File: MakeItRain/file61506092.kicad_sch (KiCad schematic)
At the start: 11 parts, among them Q10 2N7000, Q11 2N7000, Q12 IRF9Z34NPBF

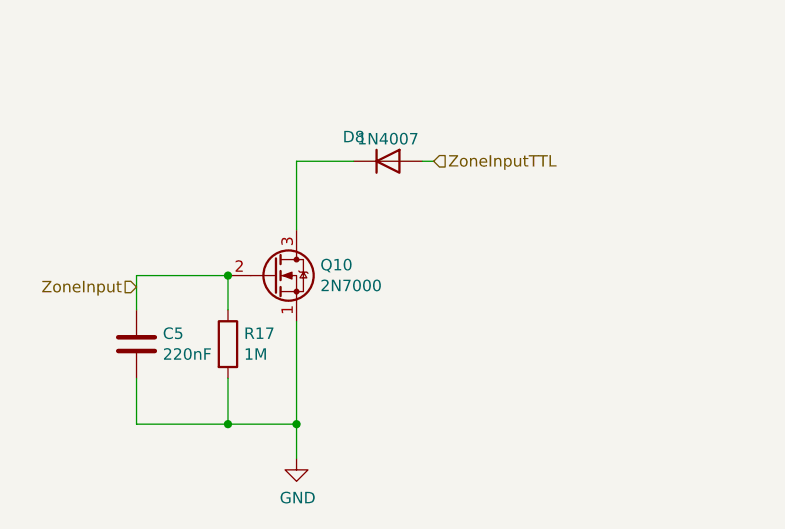
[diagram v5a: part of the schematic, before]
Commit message: working on pin reassignment to fix the stupid stupid ways that esp32 are designed in hardware that require much in way of digging through docs cause not all gpio are created equal.
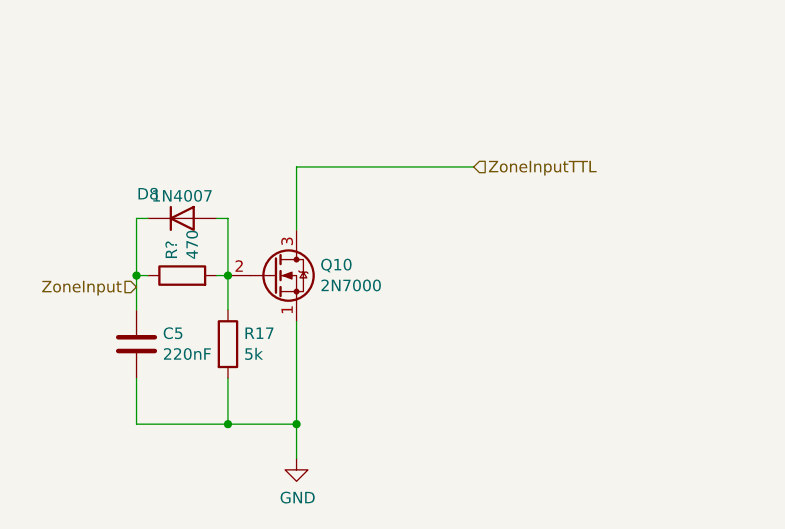
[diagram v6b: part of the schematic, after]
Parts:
- added R?: 470, Resistor_THT:R_Axial_DIN0207_L6.3mm_D2.5mm_P2.54mm_Vertical, symbol Device:R
- R17: value 1M -> 5k
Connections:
- net ZoneInput: now also D8.1 (K), R?.1; no longer Q10.2 (G), R17.1
- net ZoneInputTTL: now also Q10.3 (D); no longer D8.2 (A)
- new net: D8.2 (A), Q10.2 (G), R17.1, R?.2
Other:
- moved on the sheet: D8
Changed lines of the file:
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@@
   (junction (at 125.73 121.92) (diameter 0) (color 0 0 0 0)
   )
+  (junction (at 44.45 76.2) (diameter 0) (color 0 0 0 0)
+  )
   (junction (at 62.23 92.71) (diameter 0) (color 0 0 0 0)
   )
   (junction (at 135.89 55.88) (diameter 0) (color 0 0 0 0)
   )
+  (wire (pts (xy 44.45 76.2) (xy 45.72 76.2))
+    (stroke (width 0) (type default) (color 0 0 0 0))
+  )
   (wire (pts (xy 146.05 55.88) (xy 135.89 55.88))
     (stroke (width 0) (type default) (color 0 0 0 0))
@@
     (stroke (width 0) (type default) (color 0 0 0 0))
   )
-  (wire (pts (xy 62.23 63.5) (xy 62.23 71.12))
-    (stroke (width 0) (type default) (color 0 0 0 0))
-  )
   (wire (pts (xy 125.73 125.73) (xy 125.73 121.92))
     (stroke (width 0) (type default) (color 0 0 0 0))
@@
     (stroke (width 0) (type default) (color 0 0 0 0))
   )
-  (wire (pts (xy 44.45 76.2) (xy 54.61 76.2))
+  (wire (pts (xy 45.72 69.85) (xy 44.45 69.85))
     (stroke (width 0) (type default) (color 0 0 0 0))
   )
@@
     (stroke (width 0) (type default) (color 0 0 0 0))
   )
+  (wire (pts (xy 62.23 71.12) (xy 62.23 64.135))
+    (stroke (width 0) (type default) (color 0 0 0 0))
+  )
   (wire (pts (xy 135.89 55.88) (xy 125.73 55.88))
     (stroke (width 0) (type default) (color 0 0 0 0))
@@
     (stroke (width 0) (type default) (color 0 0 0 0))
   )
+  (wire (pts (xy 62.23 64.135) (xy 81.915 64.135))
+    (stroke (width 0) (type default) (color 0 0 0 0))
+  )
   (wire (pts (xy 142.24 121.92) (xy 125.73 121.92))
     (stroke (width 0) (type default) (color 0 0 0 0))
@@
     (stroke (width 0) (type default) (color 0 0 0 0))
   )
-  (wire (pts (xy 76.2 63.5) (xy 77.47 63.5))
-    (stroke (width 0) (type default) (color 0 0 0 0))
-  )
   (wire (pts (xy 118.11 121.92) (xy 125.73 121.92))
     (stroke (width 0) (type default) (color 0 0 0 0))
   )
-  (wire (pts (xy 68.58 63.5) (xy 62.23 63.5))
+  (wire (pts (xy 53.34 69.85) (xy 54.61 69.85))
+    (stroke (width 0) (type default) (color 0 0 0 0))
+  )
+  (wire (pts (xy 54.61 69.85) (xy 54.61 76.2))
     (stroke (width 0) (type default) (color 0 0 0 0))
   )
@@
   )
   (wire (pts (xy 146.05 92.71) (xy 146.05 90.17))
+    (stroke (width 0) (type default) (color 0 0 0 0))
+  )
+  (wire (pts (xy 44.45 69.85) (xy 44.45 76.2))
+    (stroke (width 0) (type default) (color 0 0 0 0))
+  )
+  (wire (pts (xy 53.34 76.2) (xy 54.61 76.2))
     (stroke (width 0) (type default) (color 0 0 0 0))
   )
@@
     (effects (font (size 1.27 1.27)) (justify left))
   )
-  (hierarchical_label "ZoneInputTTL" (shape input) (at 77.47 63.5 0)
+  (hierarchical_label "ZoneInputTTL" (shape input) (at 81.915 64.135 0)
     (effects (font (size 1.27 1.27)) (justify left))
   )
@@
       (effects (font (size 1.27 1.27)) (justify left))
     )
-    (property "Value" "1M" (id 1) (at 56.388 84.963 0)
+    (property "Value" "5k" (id 1) (at 56.388 84.963 0)
       (effects (font (size 1.27 1.27)) (justify left))
     )
@@
     (pin "2")
   )
-  (symbol (lib_id "Diode:1N4007") (at 72.39 63.5 0)
-    (in_bom yes) (on_board yes)
-    (property "Reference" "D8" (id 0) (at 68.58 60.8035 0))
-    (property "Value" "1N4007" (id 1) (at 72.39 61.0386 0))
-    (property "Footprint" "Diode_THT:D_DO-41_SOD81_P10.16mm_Horizontal" (id 2) (at 72.39 67.945 0)
-      (effects (font (size 1.27 1.27)) hide)
-    )
-    (property "Datasheet" "http://www.vishay.com/docs/88503/1n4001.pdf" (id 3) (at 72.39 63.5 0)
-      (effects (font (size 1.27 1.27)) hide)
-    )
+  (symbol (lib_id "Diode:1N4007") (at 49.53 69.85 0)
+    (in_bom yes) (on_board yes)
+    (property "Reference" "D8" (id 0) (at 45.72 67.1535 0))
+    (property "Value" "1N4007" (id 1) (at 49.53 67.3886 0))
+    (property "Footprint" "Diode_THT:D_DO-41_SOD81_P10.16mm_Horizontal" (id 2) (at 49.53 74.295 0)
+      (effects (font (size 1.27 1.27)) hide)
+    )
+    (property "Datasheet" "http://www.vishay.com/docs/88503/1n4001.pdf" (id 3) (at 49.53 69.85 0)
+      (effects (font (size 1.27 1.27)) hide)
+    )
+    (pin "1")
+    (pin "2")
+  )
+  (symbol (lib_id "Device:R") (at 49.53 76.2 90)
+    (in_bom yes) (on_board yes)
+    (property "Reference" "R?" (id 0) (at 48.3616 74.422 0)
+      (effects (font (size 1.27 1.27)) (justify left))
+    )
+    (property "Value" "470" (id 1) (at 50.673 74.422 0)
+      (effects (font (size 1.27 1.27)) (justify left))
+    )
+    (property "Footprint" "Resistor_THT:R_Axial_DIN0207_L6.3mm_D2.5mm_P2.54mm_Vertical" (id 2) (at 49.53 77.978 90)
+      (effects (font (size 1.27 1.27)) hide)
+    )
+    (property "Datasheet" "~" (id 3) (at 49.53 76.2 0)
+      (effects (font (size 1.27 1.27)) hide)
+    )

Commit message: min updates on schem. wip
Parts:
- gave numbers to parts that had none: 1
- renumbered C5 to C2, D8 to D2, D7 to D3, Q10 to Q1, Q11 to Q2, Q12 to Q3, R17 to R5, R18 to R6, R19 to R7, R20 to R8, Z8 to Z5
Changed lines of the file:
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@@
   (symbol (lib_id "Transistor_FET:2N7000") (at 59.69 76.2 0)
     (in_bom yes) (on_board yes)
-    (property "Reference" "Q10" (id 0) (at 64.8716 75.0316 0)
+    (property "Reference" "Q1" (id 0) (at 64.8716 75.0316 0)
       (effects (font (size 1.27 1.27)) (justify left))
     )
@@
   (symbol (lib_id "Device:R") (at 54.61 83.82 0)
     (in_bom yes) (on_board yes)
-    (property "Reference" "R17" (id 0) (at 56.388 82.6516 0)
+    (property "Reference" "R5" (id 0) (at 56.388 82.6516 0)
       (effects (font (size 1.27 1.27)) (justify left))
     )
@@
   (symbol (lib_id "Transistor_FET:2N7000") (at 123.19 105.41 0)
     (in_bom yes) (on_board yes)
-    (property "Reference" "Q11" (id 0) (at 128.3716 104.2416 0)
+    (property "Reference" "Q2" (id 0) (at 128.3716 104.2416 0)
       (effects (font (size 1.27 1.27)) (justify left))
     )
@@
   (symbol (lib_id "Device:R") (at 118.11 118.11 0)
     (in_bom yes) (on_board yes)
-    (property "Reference" "R18" (id 0) (at 119.888 116.9416 0)
+    (property "Reference" "R6" (id 0) (at 119.888 116.9416 0)
       (effects (font (size 1.27 1.27)) (justify left))
     )
@@
   (symbol (lib_id "Device:R") (at 125.73 91.44 0)
     (in_bom yes) (on_board yes)
-    (property "Reference" "R20" (id 0) (at 127.508 90.2716 0)
+    (property "Reference" "R8" (id 0) (at 127.508 90.2716 0)
       (effects (font (size 1.27 1.27)) (justify left))
     )
@@
   (symbol (lib_id "Device:R") (at 125.73 78.74 0)
     (in_bom yes) (on_board yes)
-    (property "Reference" "R19" (id 0) (at 127.508 77.5716 0)
+    (property "Reference" "R7" (id 0) (at 127.508 77.5716 0)
       (effects (font (size 1.27 1.27)) (justify left))
     )
@@
   (symbol (lib_id "SamacSys_Parts:IRF9Z34NPBF") (at 138.43 85.09 0)
     (in_bom yes) (on_board yes)
-    (property "Reference" "Q12" (id 0) (at 149.352 81.3816 0)
+    (property "Reference" "Q3" (id 0) (at 149.352 81.3816 0)
       (effects (font (size 1.27 1.27)) (justify left))
     )
@@
   (symbol (lib_id "Device:D_Schottky") (at 142.24 101.6 270)
     (in_bom yes) (on_board yes)
-    (property "Reference" "D7" (id 0) (at 144.272 100.4316 90)
+    (property "Reference" "D3" (id 0) (at 144.272 100.4316 90)
       (effects (font (size 1.27 1.27)) (justify left))
     )
@@
   (symbol (lib_id "SamacSys_Parts:BZX79C10") (at 135.89 62.23 90) (mirror x)
     (in_bom yes) (on_board yes)
-    (property "Reference" "Z8" (id 0) (at 139.192 68.6816 90)
+    (property "Reference" "Z5" (id 0) (at 139.192 68.6816 90)
       (effects (font (size 1.27 1.27)) (justify right))
     )
@@
   (symbol (lib_id "Device:C") (at 44.45 83.82 0)
     (in_bom yes) (on_board yes)
-    (property "Reference" "C5" (id 0) (at 47.371 82.6516 0)
+    (property "Reference" "C2" (id 0) (at 47.371 82.6516 0)
       (effects (font (size 1.27 1.27)) (justify left))
     )
@@
   (symbol (lib_id "Diode:1N4007") (at 49.53 69.85 0)
     (in_bom yes) (on_board yes)
-    (property "Reference" "D8" (id 0) (at 45.72 67.1535 0))
+    (property "Reference" "D2" (id 0) (at 45.72 67.1535 0))
     (property "Value" "1N4007" (id 1) (at 49.53 67.3886 0))
     (property "Footprint" "Diode_THT:D_DO-41_SOD81_P10.16mm_Horizontal" (id 2) (at 49.53 74.295 0)
@@
   (symbol (lib_id "Device:R") (at 49.53 76.2 90)
     (in_bom yes) (on_board yes)
-    (property "Reference" "R?" (id 0) (at 48.3616 74.422 0)
-      (effects (font (size 1.27 1.27)) (justify left))
-    )
+    (property "Reference" "R1" (id 0) (at 48.3616 74.422 0)
+      (effects (font (size 1.27 1.27)) (justify left))
+    )

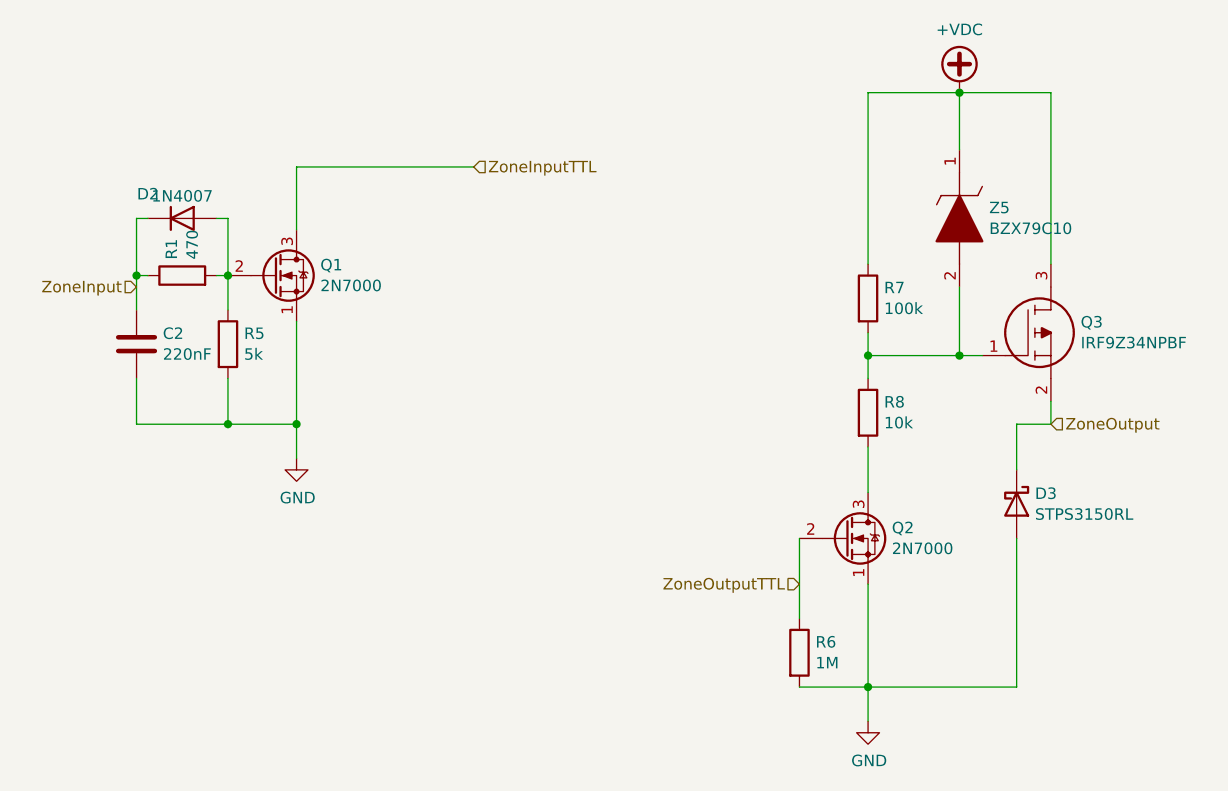
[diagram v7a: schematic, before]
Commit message: starting to add in the mcp23008 to get around the lack of pins or "special" pins that will fuck up designs. stupid ESP32s
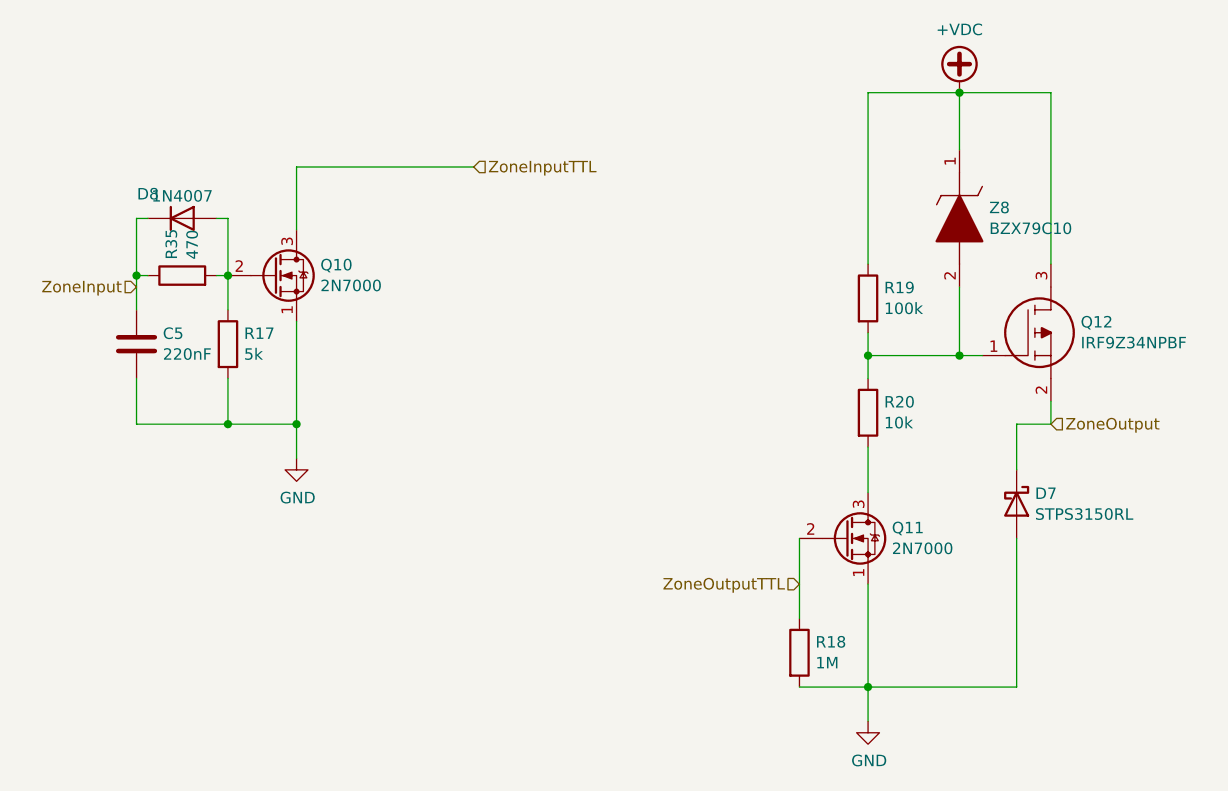
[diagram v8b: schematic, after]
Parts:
- renumbered C2 to C5, D3 to D7, D2 to D8, Q1 to Q10, Q2 to Q11, Q3 to Q12, R5 to R17, R6 to R18, R7 to R19, R8 to R20, R1 to R35, Z5 to Z8
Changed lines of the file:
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@@
   (symbol (lib_id "Transistor_FET:2N7000") (at 59.69 76.2 0)
     (in_bom yes) (on_board yes)
-    (property "Reference" "Q1" (id 0) (at 64.8716 75.0316 0)
+    (property "Reference" "Q10" (id 0) (at 64.8716 75.0316 0)
       (effects (font (size 1.27 1.27)) (justify left))
     )
@@
   (symbol (lib_id "Device:R") (at 54.61 83.82 0)
     (in_bom yes) (on_board yes)
-    (property "Reference" "R5" (id 0) (at 56.388 82.6516 0)
+    (property "Reference" "R17" (id 0) (at 56.388 82.6516 0)
       (effects (font (size 1.27 1.27)) (justify left))
     )
@@
   (symbol (lib_id "Transistor_FET:2N7000") (at 123.19 105.41 0)
     (in_bom yes) (on_board yes)
-    (property "Reference" "Q2" (id 0) (at 128.3716 104.2416 0)
+    (property "Reference" "Q11" (id 0) (at 128.3716 104.2416 0)
       (effects (font (size 1.27 1.27)) (justify left))
     )
@@
   (symbol (lib_id "Device:R") (at 118.11 118.11 0)
     (in_bom yes) (on_board yes)
-    (property "Reference" "R6" (id 0) (at 119.888 116.9416 0)
+    (property "Reference" "R18" (id 0) (at 119.888 116.9416 0)
       (effects (font (size 1.27 1.27)) (justify left))
     )
@@
   (symbol (lib_id "Device:R") (at 125.73 91.44 0)
     (in_bom yes) (on_board yes)
-    (property "Reference" "R8" (id 0) (at 127.508 90.2716 0)
+    (property "Reference" "R20" (id 0) (at 127.508 90.2716 0)
       (effects (font (size 1.27 1.27)) (justify left))
     )
@@
   (symbol (lib_id "Device:R") (at 125.73 78.74 0)
     (in_bom yes) (on_board yes)
-    (property "Reference" "R7" (id 0) (at 127.508 77.5716 0)
+    (property "Reference" "R19" (id 0) (at 127.508 77.5716 0)
       (effects (font (size 1.27 1.27)) (justify left))
     )
@@
   (symbol (lib_id "SamacSys_Parts:IRF9Z34NPBF") (at 138.43 85.09 0)
     (in_bom yes) (on_board yes)
-    (property "Reference" "Q3" (id 0) (at 149.352 81.3816 0)
+    (property "Reference" "Q12" (id 0) (at 149.352 81.3816 0)
       (effects (font (size 1.27 1.27)) (justify left))
     )
@@
   (symbol (lib_id "Device:D_Schottky") (at 142.24 101.6 270)
     (in_bom yes) (on_board yes)
-    (property "Reference" "D3" (id 0) (at 144.272 100.4316 90)
+    (property "Reference" "D7" (id 0) (at 144.272 100.4316 90)
       (effects (font (size 1.27 1.27)) (justify left))
     )
@@
   (symbol (lib_id "SamacSys_Parts:BZX79C10") (at 135.89 62.23 90) (mirror x)
     (in_bom yes) (on_board yes)
-    (property "Reference" "Z5" (id 0) (at 139.192 68.6816 90)
+    (property "Reference" "Z8" (id 0) (at 139.192 68.6816 90)
       (effects (font (size 1.27 1.27)) (justify right))
     )
@@
   (symbol (lib_id "Device:C") (at 44.45 83.82 0)
     (in_bom yes) (on_board yes)
-    (property "Reference" "C2" (id 0) (at 47.371 82.6516 0)
+    (property "Reference" "C5" (id 0) (at 47.371 82.6516 0)
       (effects (font (size 1.27 1.27)) (justify left))
     )
@@
   (symbol (lib_id "Diode:1N4007") (at 49.53 69.85 0)
     (in_bom yes) (on_board yes)
-    (property "Reference" "D2" (id 0) (at 45.72 67.1535 0))
+    (property "Reference" "D8" (id 0) (at 45.72 67.1535 0))
     (property "Value" "1N4007" (id 1) (at 49.53 67.3886 0))
     (property "Footprint" "Diode_THT:D_DO-41_SOD81_P10.16mm_Horizontal" (id 2) (at 49.53 74.295 0)
@@
   (symbol (lib_id "Device:R") (at 49.53 76.2 90)
     (in_bom yes) (on_board yes)
-    (property "Reference" "R1" (id 0) (at 48.3616 74.422 0)
-      (effects (font (size 1.27 1.27)) (justify left))
-    )
+    (property "Reference" "R35" (id 0) (at 48.3616 74.422 0)
+      (effects (font (size 1.27 1.27)) (justify left))
+    )
